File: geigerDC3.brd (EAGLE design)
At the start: 75 x 90 mm, 159 parts, among them IC1 REG1117, Q1 BC858ALT1SMD, Q2 12MHz, Q3 32768KHz, SW1 SWT6-MSMT, SW2 SWT6-MSMT, SW3 SWT6-MSMT, SW4 SWT6-MSMT, SW5 SWT6-MSMT, SW6 SWT6-MSMT, T1 IRLML5203, T10 IRLML5203, T11 IRLML2502, T12 IRLML5203, T13 IRLML2502, T14 BC850, T15 BC858ALT1SMD, T16 BC850, T2 IRLML2502, T3 IRLML5203, T4 IRLML5203, T5 IRLML5203, T6 IRLML2502, T7 BC850, T8 IRLML2502, T9 BC858ALT1SMD, U1 M95256-WMN6TP, U2 STM32F103C8T6, X1 MINI-USB-32005-201

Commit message: start routing
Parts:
- removed C14, C7: (no value), rcl:C2220K
- removed D6, D7: (no value), diode:DO214BA
- removed JP2: BAT, pinhead:1X02/90
- removed JP4: STATUS_LED, pinhead:1X02/90
- removed Q1: BC858ALT1SMD, transistor-pnp:SOT23-BEC
- removed R38: 10kOm, rcl:R0402
- removed U$1: MCP73831T-4ADI/OT, MCP73831T-4ADI_OT:SOT95P280X145-5N
- added J1: B2B-XH-A(LF)(SN), B2B-XH-A_LF__SN_:JST_B2B-XH-A(LF)(SN)
- added L5: (no value), SparkFun:0805
- added LED1: LS_T679-D2E2-1, led:PLCC2
- added T18: BC858ALT1SMD, transistor-pnp:SOT23-BEC
- added U3: MCP73831T-4ADI/OT, MCP73831T-4ADI_OT:SOT95P280X145-5N
- C44: device rcl:C0805 -> rcl:C0402
- JP1, JP6: device pinhead:1X03/90 -> pinhead:1X03
- JP3: device pinhead:1X02/90 -> pinhead:1X02
- JP7: device pinhead:1X05/90 -> pinhead:1X05
- SG1: value BUZZERSMD2 -> BUZZERSMD2-KIT; device SparkFun:BUZZER-CCV -> SparkFun:BUZZER-CCV-KIT
- moved R1 209.5 mm to (63.1, 55.9), turned to 180 degrees
- moved T7 203.9 mm to (59.8, 33.6), turned to 270 degrees
- moved C42 194.9 mm to (37.5, 32.0)
- moved U$3 194.1 mm to (59.1, 70.4), turned to 180 degrees
- moved R16 194.0 mm to (70.0, 23.7), turned to 270 degrees
- moved C43 191.8 mm to (27.5, 32.0)
- moved C22 189.6 mm to (67.1, 78.2), turned to 270 degrees
- moved R50 188.4 mm to (31.0, 29.5), turned to 270 degrees
- moved R48 186.4 mm to (46.5, 29.5), turned to 270 degrees
- moved D10 184.2 mm to (51.0, 48.3), turned to 90 degrees
- moved C25 182.8 mm to (47.9, 68.3)
- moved R49 180.8 mm to (36.5, 39.5), turned to 270 degrees
- moved R22 180.1 mm to (59.7, 56.7), turned to 90 degrees
- moved R7 179.5 mm to (53.0, 19.0), turned to 90 degrees
- moved C24 175.1 mm to (49.5, 79.7), turned to 180 degrees
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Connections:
- removed net +6V: JP2.2
- removed net N$75: R48.1, SW4.1, SW4.2
- removed net N$82: R47.1, SW5.1, SW5.2
- new net N$91: C22.+, L2.2, L5.1
- net +12V: now also J1.2
- net +3V3: now also T18.E; no longer Q1.E, R38.1
- net +5V: now also U3.4; no longer U$1.4
- net GND: now also J1.1, LED1.C, U3.2; no longer JP2.1, JP4.2, U$1.2
- net N$100: now also U3.5; no longer U$1.5
- net N$108: now also L5.2; no longer C22.+, L2.2
- net N$11: no longer R38.2
- net N$15: now also U3.3; no longer U$1.3
- net N$26: now also C17.1, R13.2, R7.1; no longer C14.1, D6.A
- net N$38: now also C43.1, R47.1, SW5.1, SW5.2; no longer C7.2, D6.C, D7.A
- net N$49: no longer C7.1
- net N$50: now also C44.1, R48.1, SW4.1, SW4.2; no longer C14.2, C17.1, D7.C, R13.2, R7.1
- net N$62: now also T18.B; no longer Q1.B
- net N$64: now also T18.C; no longer Q1.C
- net N$72: no longer C45.1
- net N$73: now also C46.1
- net N$76: now also C45.1
- net N$80: no longer C43.1
- net N$81: no longer C44.1
- net N$83: no longer C46.1
- net N$96: now also LED1.A; no longer JP4.1
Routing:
- net GND: track 0.00 -> 271.1 mm, vias 0 -> 8
- net +3V3: track 0.00 -> 93.1 mm
- net +5V/2: track 0.00 -> 91.9 mm, vias 0 -> 4
- net N$12: track 0.00 -> 58.6 mm
- net N$11: track 0.00 -> 57.8 mm
- net N$32: track 0.00 -> 52.3 mm, vias 0 -> 2
- net N$31: track 0.00 -> 48.6 mm
- net +5V: track 0.00 -> 44.8 mm, vias 0 -> 2
- net N$66: track 0.00 -> 37.0 mm
- net N$33: track 0.00 -> 33.4 mm
- net N$26: track 0.00 -> 29.4 mm
- net N$25: track 0.00 -> 29.3 mm, vias 0 -> 2
- net N$27: track 0.00 -> 28.2 mm, vias 0 -> 2
- net N$2: track 0.00 -> 25.5 mm
- net N$70: track 0.00 -> 22.2 mm
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- added copper zone on layer 1, net GND
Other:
- outline, holes or cut-outs redrawn

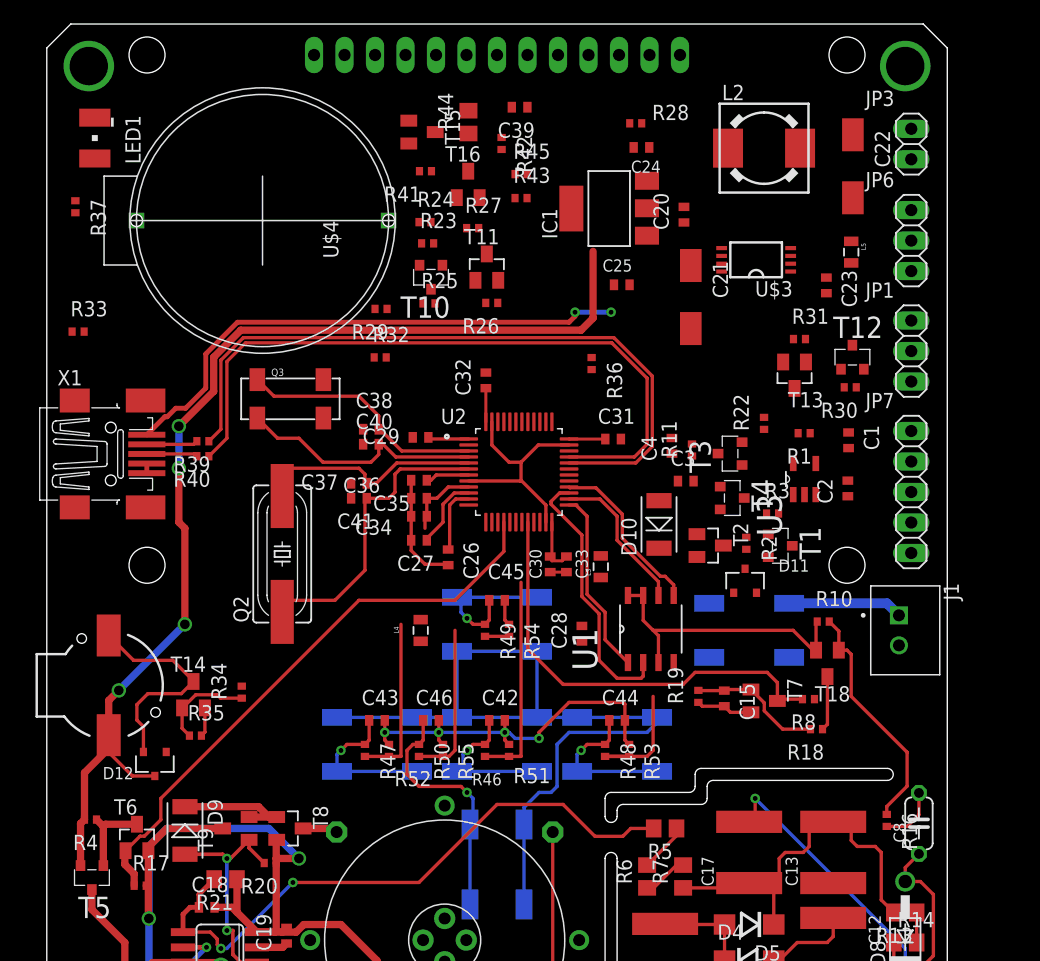
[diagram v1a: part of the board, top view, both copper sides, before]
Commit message: change MCU orientation
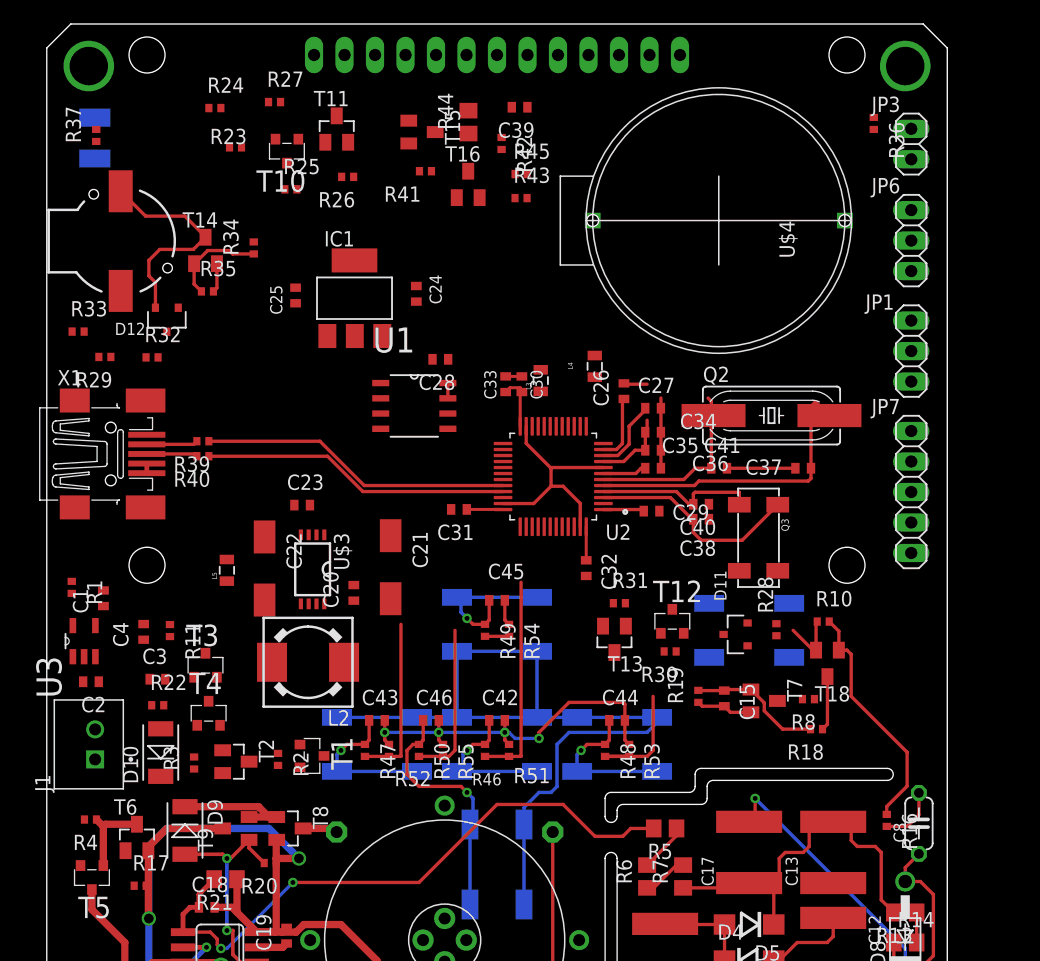
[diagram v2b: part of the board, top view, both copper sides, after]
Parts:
- moved J1 68.7 mm to (3.50, 30.0), turned to 90 degrees
- moved C2 65.1 mm to (3.68, 35.2), turned to 180 degrees
- moved C1 63.4 mm to (4.72, 42.2), turned to 90 degrees
- moved R1 62.3 mm to (2.08, 43.1), turned to 270 degrees
- moved U3 61.5 mm to (3.11, 38.6)
- moved C22 59.4 mm to (18.1, 44.6)
- moved L5 58.4 mm to (15.0, 44.5), turned to 90 degrees
- moved L2 57.2 mm to (21.8, 36.8), turned to 180 degrees
- moved R22 55.7 mm to (9.24, 33.3), turned to 0 degrees
- moved R3 52.5 mm to (12.3, 28.4), turned to 90 degrees
- moved C23 47.3 mm to (21.3, 49.9), turned to 0 degrees
- moved T4 47.2 mm to (13.5, 32.6), turned to 0 degrees
- moved T3 47.1 mm to (13.2, 36.6), turned to 0 degrees
- moved C3 47.0 mm to (9.22, 35.4)
- moved C4 46.7 mm to (8.07, 39.4)
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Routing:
- net +5V/2: track 91.9 -> 0.00 mm, vias 4 -> 0
- net N$31: track 48.6 -> 0.00 mm
- net +5V: track 44.8 -> 0.00 mm, vias 2 -> 0
- net N$66: track 37.0 -> 0.00 mm
- net N$12: track 58.6 -> 26.0 mm
- net N$11: track 57.8 -> 25.7 mm
- net N$70: track 22.2 -> 0.00 mm
- net +3V3: track 93.1 -> 75.3 mm
- net N$74: track 15.5 -> 0.00 mm
- net N$69: track 14.1 -> 0.00 mm
- net N$71: track 12.6 -> 0.00 mm
- net N$2: track 25.5 -> 15.6 mm
- net N$7: track 20.7 -> 13.7 mm
- net N$4: track 19.3 -> 25.7 mm
- net GND: track 271.1 -> 265.7 mm
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
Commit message: Almost all routing
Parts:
- removed D8: TUBE, diode:DO41-10
- removed U$4: CR2032, cr2032:CR2032-20MM
- added TUBE: TUBE, XH:XH-B3B
- added U$1: DS1092-10-W6L, batteries:DS1092-10-W6L
- moved R33 38.0 mm to (40.4, 68.6), turned to 180 degrees
- moved R24 14.2 mm to (21.5, 71.0), turned to 90 degrees
- moved C8 9.57 mm to (63.9, 27.4), turned to 0 degrees
- moved R13 8.00 mm to (71.5, 24.0)
- moved R14 8.00 mm to (71.5, 21.5)
- moved R15 8.00 mm to (71.5, 19.0)
- moved R23 5.83 mm to (18.7, 84.7)
- moved R43 5.70 mm to (35.0, 72.0), turned to 90 degrees
- moved R45 5.59 mm to (34.5, 75.0), turned to 270 degrees
- moved R27 5.58 mm to (21.5, 78.5), turned to 270 degrees
- moved R16 3.95 mm to (69.2, 27.5), turned to 180 degrees
- moved T16 3.50 mm to (31.6, 76.6)
- moved R42 3.04 mm to (34.9, 80.5)
- moved R41 3.00 mm to (28.5, 77.7)
- moved L4 2.94 mm to (48.5, 62.1), turned to 180 degrees
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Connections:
- net GND: now also TUBE.K, U$1.-; no longer D8.C, U$4.GND
- net N$10: now also U$1.+; no longer U$4.VCC
- net N$60: now also TUBE.A; no longer D8.A
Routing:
- net GND: track 265.7 -> 793.8 mm, vias 8 -> 11
- net +3V3: track 75.3 -> 267.2 mm, vias 0 -> 12
- net N$31: track 0.00 -> 128.6 mm, vias 0 -> 4
- net +5V/2: track 0.00 -> 116.7 mm, vias 0 -> 3
- net +5V: track 0.00 -> 66.9 mm, vias 0 -> 3
- net N$24: track 0.00 -> 66.5 mm, vias 0 -> 4
- net N$22: track 0.00 -> 64.2 mm, vias 0 -> 4
- net N$94: track 0.00 -> 62.0 mm, vias 0 -> 2
- net N$9: track 0.00 -> 60.9 mm, vias 0 -> 2
- net N$78: track 5.56 -> 65.9 mm, vias 0 -> 4
- net N$41: track 0.00 -> 58.5 mm, vias 0 -> 3
- net N$55: track 0.00 -> 54.7 mm, vias 0 -> 3
- net N$42: track 6.09 -> 59.2 mm, vias 0 -> 4
- net N$19: track 0.00 -> 51.7 mm, vias 0 -> 2
- net N$16: track 0.00 -> 50.7 mm, vias 0 -> 2
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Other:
- outline, holes or cut-outs redrawn

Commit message: Edit board and generete gerber
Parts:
- removed Q3: 32768KHz, crystal-geyer_V1_0:8.2X3.8
- added Q1: 12MHz, crystal:HC49UP
- Q2: value 12MHz -> 32768KHz; device crystal:HC49UP -> crystal-geyer_V1_0:8.2X3.8
- SG1: value BUZZERSMD2-KIT -> BUZZER; device SparkFun:BUZZER-CCV-KIT -> buzzer:BUZZER
- moved Q2 10.2 mm to (59.3, 47.2), turned to 270 degrees
- moved R45 5.15 mm to (37.0, 79.5), turned to 0 degrees
- moved R43 4.47 mm to (37.0, 68.0)
- moved SG1 0.27 mm to (6.08, 71.7), turned to 0 degrees
- moved R3 0.15 mm to (12.1, 28.4)
- moved T4 0.10 mm to (13.5, 32.7)
- renumbered IC1 to U4, U$2 to U6, U$3 to U5
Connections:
- net +5V/2: now also SG1.2; no longer SG1.+
- net N$2: now also Q1.1; no longer Q2.1
- net N$4: now also Q1.2; no longer Q2.2
- net N$5: now also Q2.4; no longer Q3.4
- net N$7: now also Q2.1; no longer Q3.1
- net N$85: now also SG1.1; no longer SG1.-
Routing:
- net N$95: track 8.26 -> 24.7 mm
- net N$97: track 31.1 -> 27.2 mm
- net +5V/2: track 116.7 -> 117.7 mm
- net GND: track 793.8 -> 793.7 mm, vias 11 -> 12
- added copper zone on layer 16, net GND
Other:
- board text added: "-"
- board text added: "BOOT"
- board text added: "G V O C I"
- board text added: "GND RX TX"
- board text added: "UART2 UART1"
